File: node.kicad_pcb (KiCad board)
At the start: 2 copper layers, 46 x 38 mm, 39 parts, among them J1 USB_B_Mini, J2 TC2030_NL, J3 FFC-0.5MM-6POS, J4 Port_1, J5 Port_2, J6 FFC-0.5MM-6POS, J7 Port_3, J8 Port_4, U1 PMIC-LDO-XC6204B332MR_SOT23-5_, U2 LP2985-5.0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

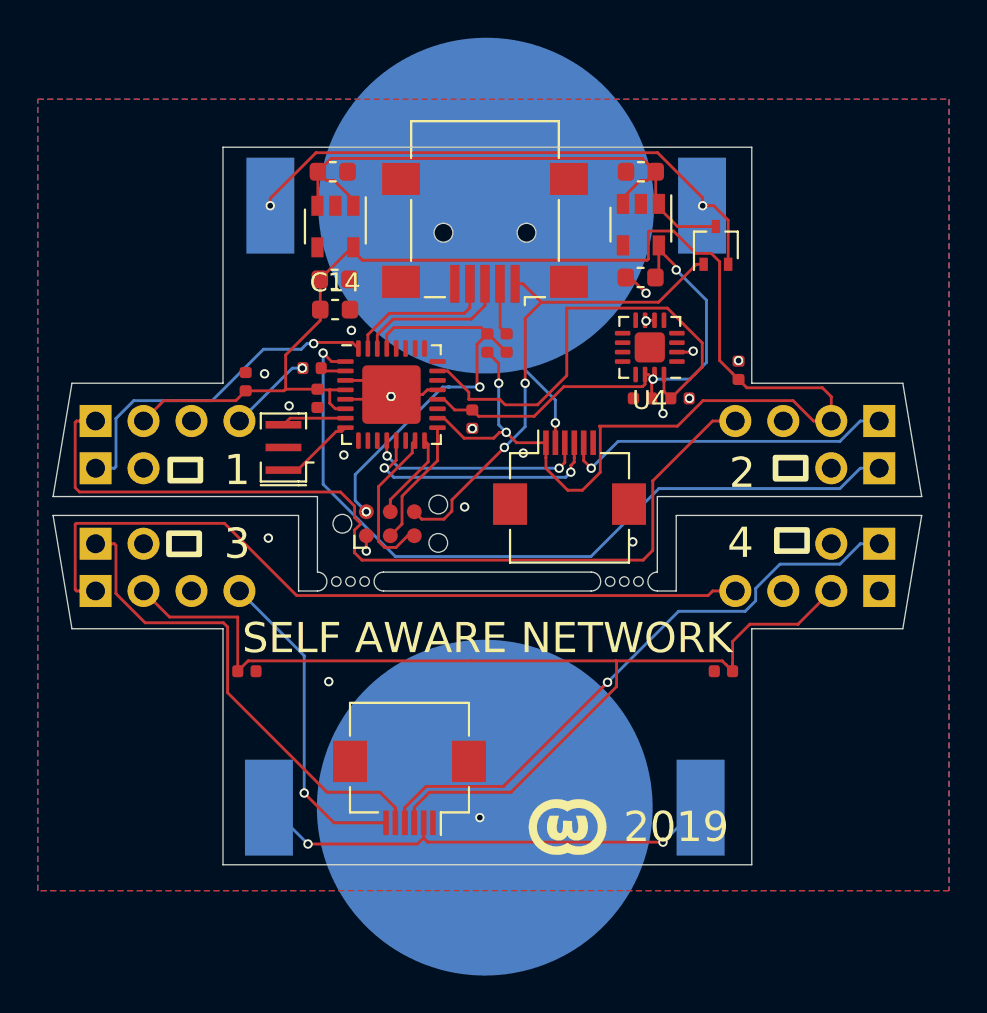
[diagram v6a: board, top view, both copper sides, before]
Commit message: Add PicoBlade connectors
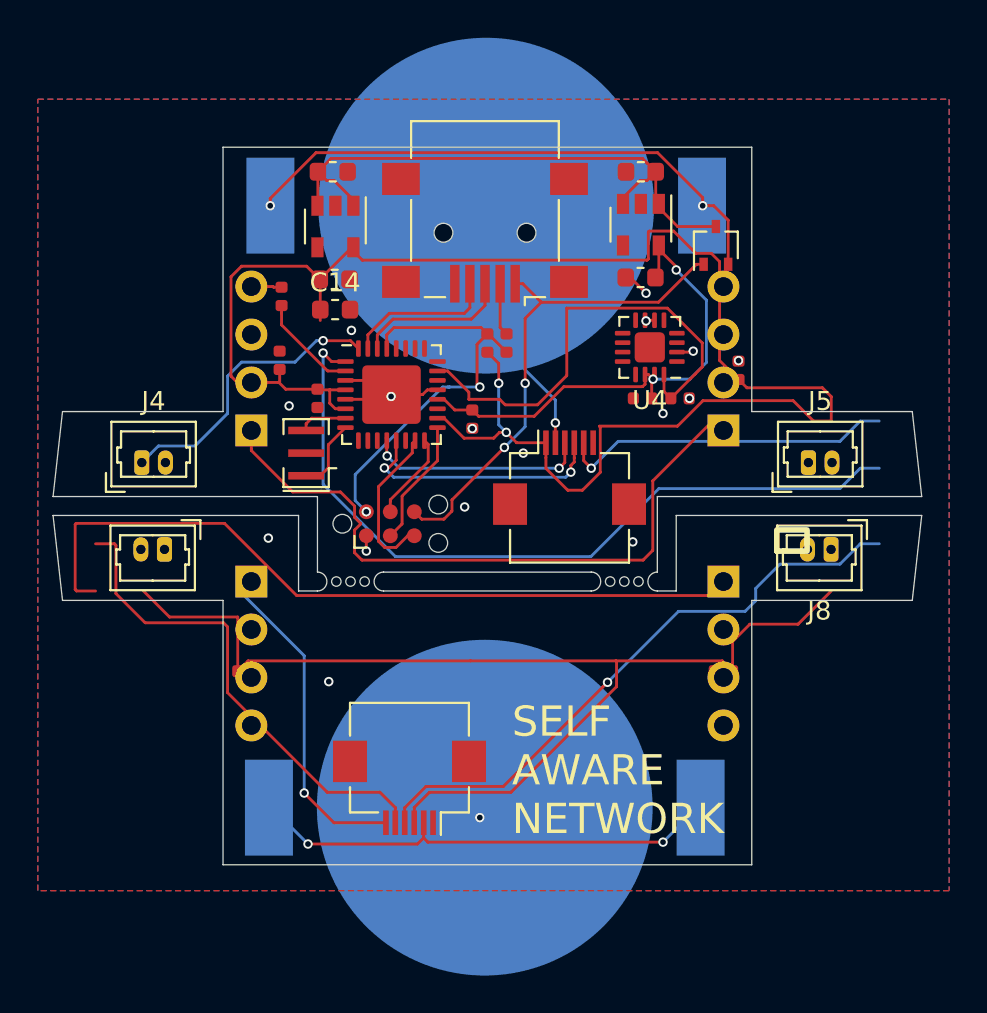
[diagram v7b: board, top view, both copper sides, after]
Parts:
- G***: moved to B.Cu
- J4, J5, J7, J8: footprint node:port -> Connector_Molex:Molex_PicoBlade_53047-0210_1x02_P1.25mm_Vertical
- moved G*** 19.0 mm to (143.8, 82.0), turned to 180 degrees
- moved D2 8.27 mm to (134.5, 78.5), turned to 180 degrees
- moved D3 8.27 mm to (159.5, 78.5), turned to 180 degrees
- moved D4 8.27 mm to (134.5, 86.5), turned to 0 degrees
- moved D5 8.27 mm to (159.5, 86.5), turned to 0 degrees
- moved R2 4.13 mm to (136.1, 71.4), turned to 270 degrees
- moved J5 3.76 mm to (164.0, 80.2), turned to 0 degrees
- moved J7 3.66 mm to (129.9, 84.8), turned to 180 degrees
- moved J8 2.57 mm to (165.2, 84.8), turned to 180 degrees
- moved J4 2.47 mm to (128.7, 80.2), turned to 0 degrees
- moved C9 2.13 mm to (136.0, 74.8)
- moved Y1 1.24 mm to (137.4, 79.7)
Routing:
- net Net-(D5-Pad1): track 0.00 -> 41.2 mm
- net Net-(D4-Pad1): track 41.2 -> 0.00 mm
- net Net-(D2-Pad1): track 48.0 -> 36.0 mm
- net Net-(R2-Pad2): track 1.34 -> 5.42 mm
- net /Top Hemisphere/BNC-1: track 18.3 -> 15.5 mm
- net +5V: track 148.2 -> 150.5 mm
- net /Top Hemisphere/DIN-TOP: track 4.49 -> 2.19 mm, vias 1 -> 0
- net Net-(U3-Pad7): track 3.43 -> 2.56 mm
- net GND: vias 19 -> 17
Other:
- outline, holes or cut-outs redrawn
- board text removed: "1"
- board text removed: "2"
- board text removed: "3"
- board text removed: "4"

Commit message: Move components and extend board (less fragile)
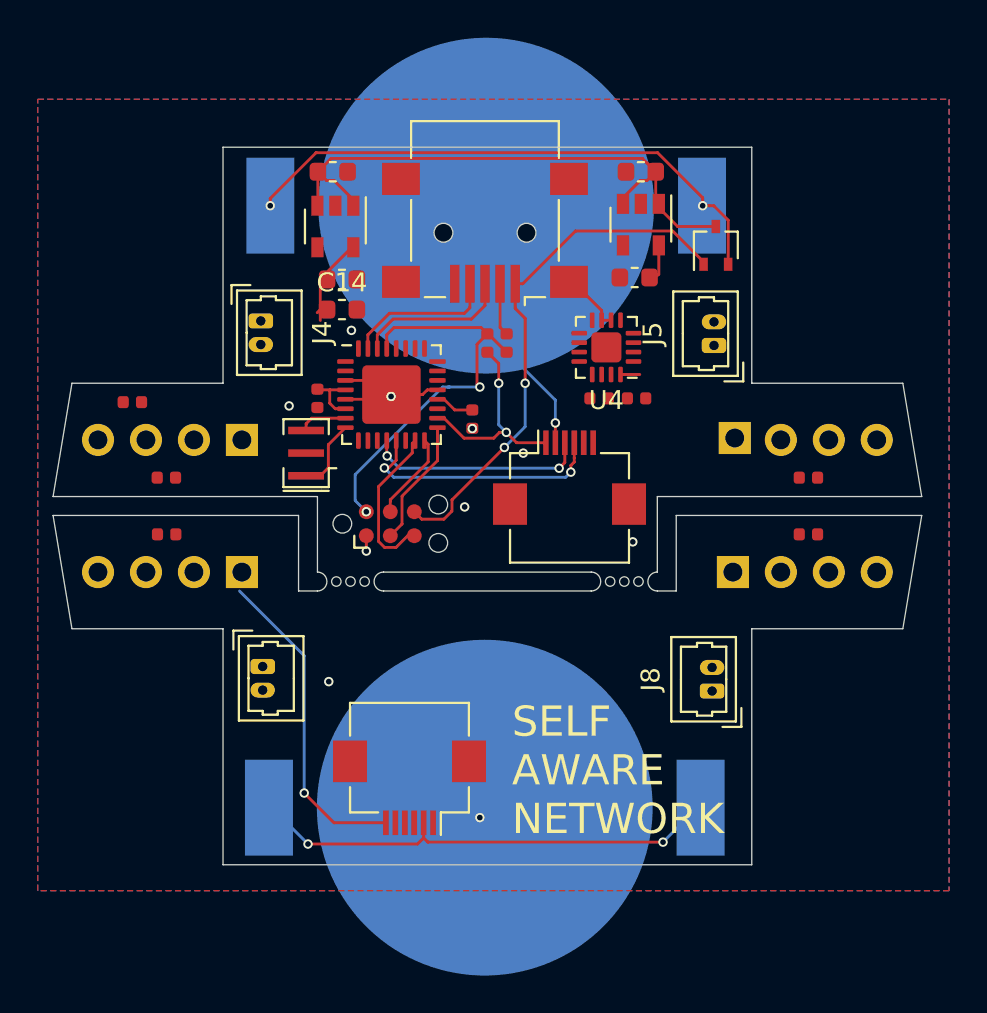
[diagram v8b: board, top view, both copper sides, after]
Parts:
- moved J4 9.79 mm to (135.0, 72.7), turned to 270 degrees
- moved J8 9.79 mm to (158.9, 92.3), turned to 90 degrees
- moved R2 9.68 mm to (128.2, 77.0), turned to 0 degrees
- moved C9 8.64 mm to (130.0, 81.0), turned to 180 degrees
- moved C13 8.53 mm to (164.0, 84.0), turned to 0 degrees
- moved C12 8.40 mm to (130.0, 84.0), turned to 180 degrees
- moved J7 8.09 mm to (135.1, 91.0), turned to 270 degrees
- moved J5 7.96 mm to (159.0, 74.0), turned to 90 degrees
- moved C11 6.78 mm to (164.0, 81.0), turned to 0 degrees
- moved C8 2.30 mm to (152.9, 76.8)
- moved C10 2.30 mm to (154.9, 76.8)
- moved U4 2.30 mm to (153.3, 74.1)
- moved D2 0.71 mm to (134.0, 79.0), turned to 270 degrees
- moved D3 0.71 mm to (160.0, 79.0), turned to 90 degrees
- moved D4 0.71 mm to (134.0, 86.0), turned to 270 degrees
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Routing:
- net +5V: track 150.5 -> 19.3 mm
- net /Top Hemisphere/BNC-2: track 41.3 -> 0.00 mm, vias 1 -> 0
- net Net-(D5-Pad1): track 41.2 -> 0.00 mm
- net Net-(D2-Pad1): track 36.0 -> 0.00 mm
- net /Bottom hemisphere/BNC-4: track 32.1 -> 0.00 mm, vias 1 -> 0
- net /Bottom hemisphere/BNC-3: track 26.0 -> 0.00 mm
- net /Top Hemisphere/Z-ACCEL: track 25.0 -> 1.02 mm
- net +3V3: track 26.4 -> 3.85 mm, vias 2 -> 0
- net /Top Hemisphere/DOUT-BOT: track 17.8 -> 0.00 mm, vias 1 -> 0
- net /Top Hemisphere/BNC-1: track 15.5 -> 0.00 mm, vias 1 -> 0
- net Net-(R2-Pad2): track 5.42 -> 0.00 mm
- net /Top Hemisphere/DIN-TOP: track 2.19 -> 0.00 mm
- net /Top Hemisphere/+5V_EXT: track 26.6 -> 28.1 mm
- net GND: track 11.4 -> 12.0 mm, vias 17 -> 10
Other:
- outline, holes or cut-outs redrawn
- board text removed: "⏚"
